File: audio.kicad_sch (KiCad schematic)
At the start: 23 parts, among them IC1 ES9218PQ, Y1 50MHz

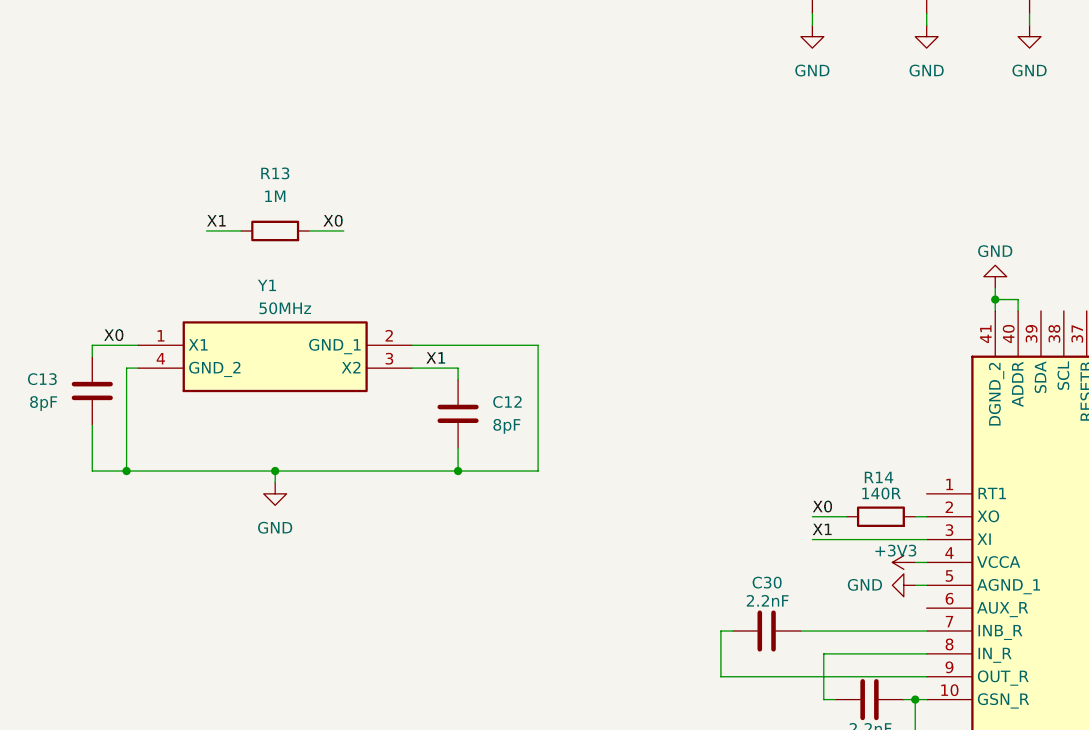
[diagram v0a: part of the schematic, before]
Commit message: changed the crystal for an oscillator, still dont know what to do wit XO pin
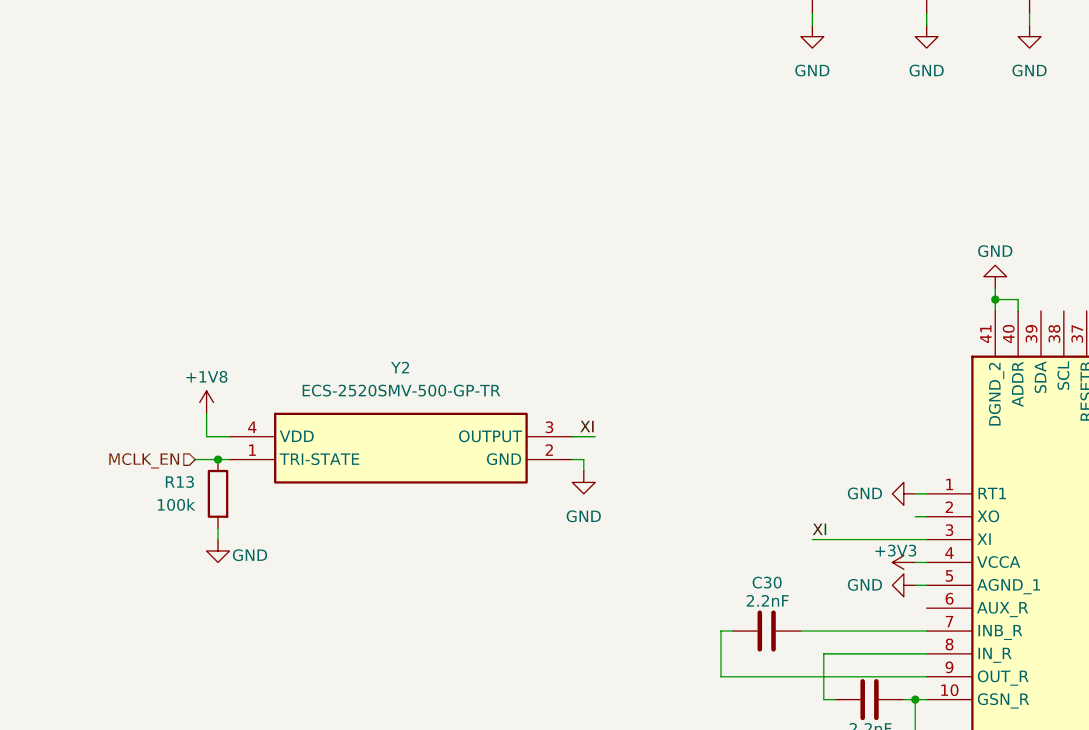
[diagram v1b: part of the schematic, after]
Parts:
- removed C12, C13: 8pF, symbol Device:C
- removed R14: 140R, symbol Device:R
- removed Y1: 50MHz, ABM10W240000MHZ8K1ZT3, symbol ABM10W-50.0000MHZ-4-B1U-T3:ABM10W-50.0000MHZ-4-B1U-T3
- added Y2: ECS-2520SMV-500-GP-TR, ECS2520SMV500GPTR, symbol ECS-2520SMV-500-GP-TR:ECS-2520SMV-500-GP-TR
- R13: value 1M -> 100k
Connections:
- net X0 is gone; now on net GND: R13.2
- net +1V8: now also Y2.4 (VDD)
- net GND: now also IC1.1 (RT1), Y2.2 (GND)
- net X1 renamed MCLK_EN
- net MCLK_EN: now also Y2.1 (TRI-STATE); no longer IC1.3 (XI)
- new net XI: IC1.3 (XI), Y2.3 (OUTPUT)

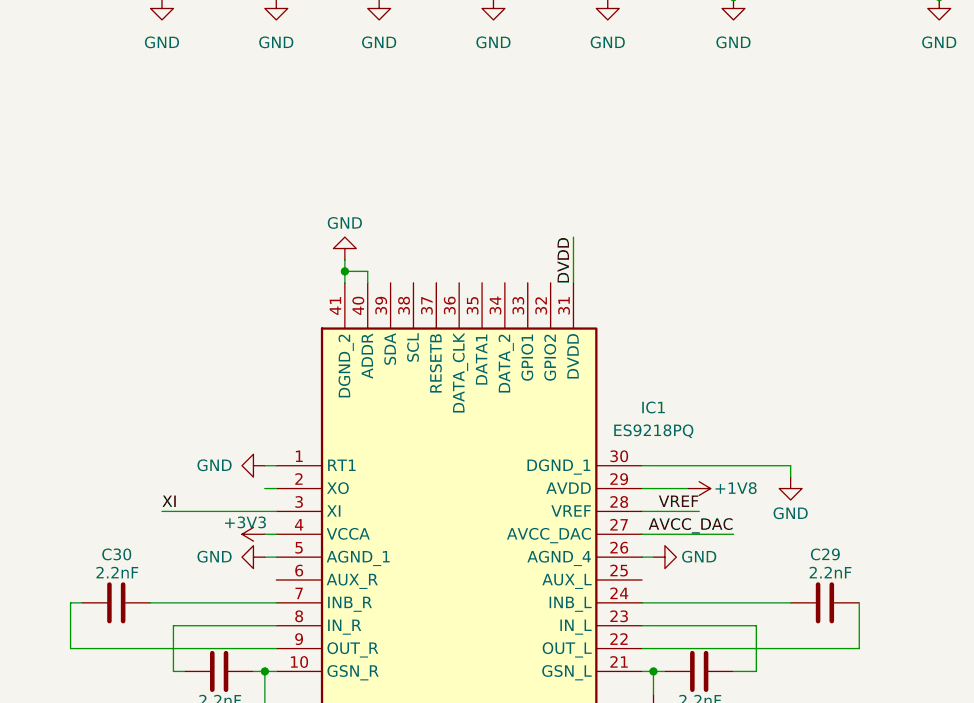
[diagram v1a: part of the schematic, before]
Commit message: added the sd card slot
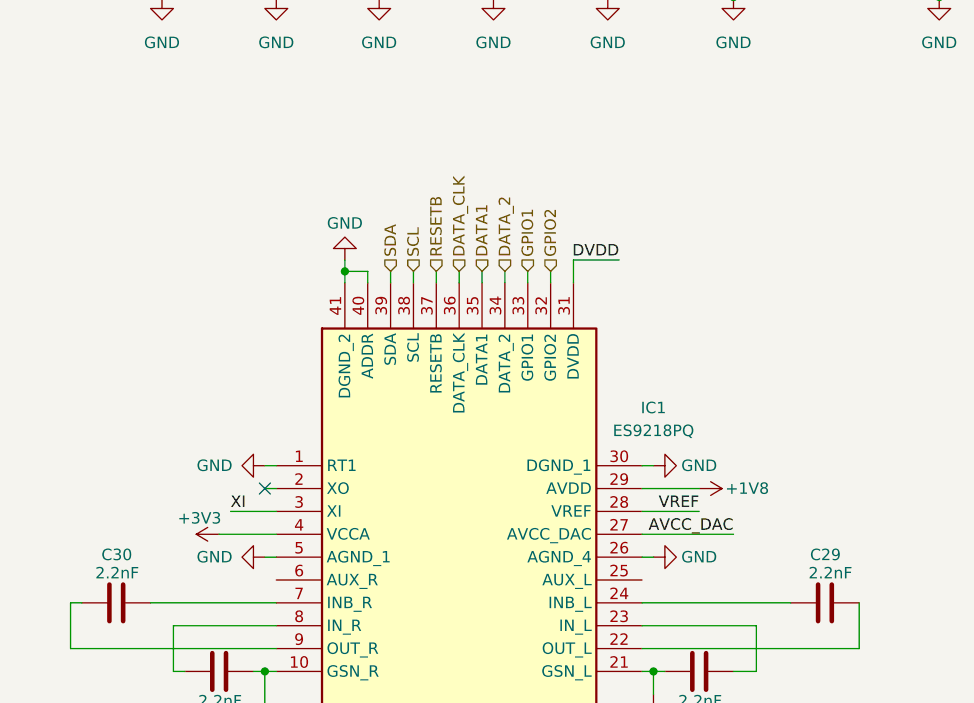
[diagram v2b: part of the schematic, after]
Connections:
- net GPIO2: now reaches IC1.32 (GPIO2)
- net GPIO1: now reaches IC1.33 (GPIO1)
- net DATA_2: now reaches IC1.34 (DATA_2)
- net DATA1: now reaches IC1.35 (DATA1)
- net DATA_CLK: now reaches IC1.36 (DATA_CLK)
- net RESETB: now reaches IC1.37 (RESETB)
- net SCL: now reaches IC1.38 (SCL)
- net SDA: now reaches IC1.39 (SDA)
- no-connect marks 0 -> 1

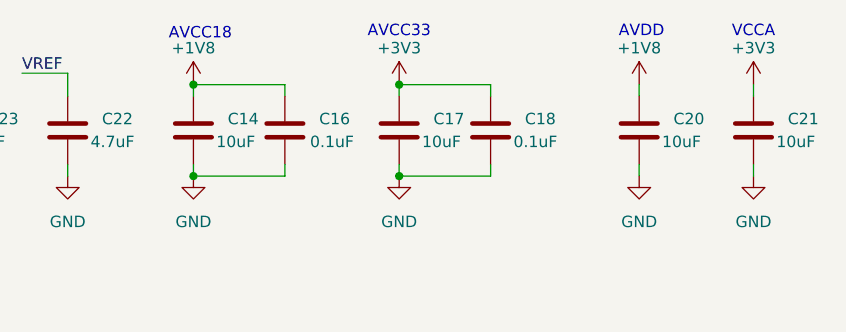
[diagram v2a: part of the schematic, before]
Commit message: made the jouranl complient, back-journaled
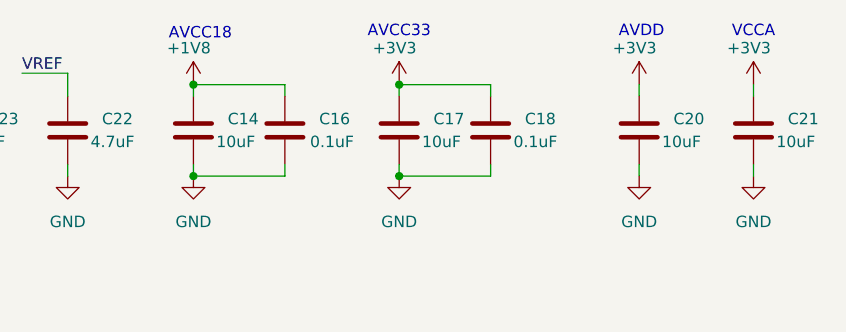
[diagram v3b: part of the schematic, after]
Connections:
- net +1V8: no longer C20.1
- net +3V3: now also C20.1
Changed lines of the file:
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@@
-	)
-	(symbol
-		(lib_id "power:+1V8")
-		(at 226.06 31.75 0)
-		(unit 1)
-		(exclude_from_sim no)
-		(in_bom yes)
-		(on_board yes)
-		(dnp no)
-		(property "Reference" "#PWR031"
-			(at 226.06 35.56 0)
-			(effects
-				(font
-					(size 1.27 1.27)
-				)
-				(hide yes)
-			)
-		)
-		(property "Value" "+1V8"
-			(at 226.06 27.686 0)
-			(effects
-				(font
-					(size 1.27 1.27)
-				)
-			)
-		)
-		(property "Footprint" ""
-			(at 226.06 31.75 0)
-			(effects
-				(font
-					(size 1.27 1.27)
-				)
-				(hide yes)
-			)
-		)
-		(property "Datasheet" ""
-			(at 226.06 31.75 0)
-			(effects
-				(font
-					(size 1.27 1.27)
-				)
-				(hide yes)
-			)
-		)
-		(property "Description" "Power symbol creates a global label with name \"+1V8\""
-			(at 226.06 31.75 0)
-			(effects
-				(font
-					(size 1.27 1.27)
-				)
-				(hide yes)
-			)
-		)
-		(pin "1"
-		)
-		(instances
-			(project "meko-pcb"
-				(path "/bdd43acd-23c1-472b-909a-8e24eb60d56d/dd2be10c-708f-4995-b13e-6fc09628a9ce"
-					(reference "#PWR031")
-					(unit 1)
-				)
-			)
-		)
 	)
 	(symbol
@@
 	)
 	(symbol
+		(lib_id "power:+3V3")
+		(at 226.06 31.75 0)
+		(unit 1)
+		(exclude_from_sim no)
+		(in_bom yes)
+		(on_board yes)
+		(dnp no)
+		(property "Reference" "#PWR03"
+			(at 226.06 35.56 0)
+			(effects
+				(font
+					(size 1.27 1.27)
+				)
+				(hide yes)
+			)
+		)
+		(property "Value" "+3V3"
+			(at 225.552 27.686 0)
+			(effects
+				(font
+					(size 1.27 1.27)
+				)
+			)
+		)
+		(property "Footprint" ""
+			(at 226.06 31.75 0)
+			(effects
+				(font
+					(size 1.27 1.27)
+				)
+				(hide yes)
+			)
+		)
+		(property "Datasheet" ""
+			(at 226.06 31.75 0)
+			(effects
+				(font
+					(size 1.27 1.27)
+				)
+				(hide yes)
+			)
+		)
+		(property "Description" "Power symbol creates a global label with name \"+3V3\""
+			(at 226.06 31.75 0)
+			(effects
+				(font
+					(size 1.27 1.27)
+				)
+				(hide yes)
+			)
+		)
+		(pin "1"
+		)
+		(instances
+			(project "meko-pcb"
+				(path "/bdd43acd-23c1-472b-909a-8e24eb60d56d/dd2be10c-708f-4995-b13e-6fc09628a9ce"
+					(reference "#PWR03")
+					(unit 1)
+				)
+			)
+		)
+	)
+	(symbol
 		(lib_id "Device:C")
 		(at 149.86 36.83 0)
@@
 			)
 		)
-		(property "Datasheet" "https://ecsxtal.com/store/pdf/ECS-2520SMV.pdf"
+		(property "Datasheet" "https://eu.mouser.com/datasheet/2/122/ECS_2520SMV-1628252.pdf"
 			(at 82.55 282.55 0)
 			(effects
@@
 		)
 		(property "Value" "+1V8"
-			(at 176.53 27.686 0)
+			(at 176.022 27.686 0)
 			(effects
 				(font
@@
 		)
 		(property "Value" "+3V3"
-			(at 199.39 27.686 0)
+			(at 198.882 27.686 0)
 			(effects
 				(font
@@
 		)
 		(property "Value" "+3V3"
-			(at 238.76 27.686 0)
-			(effects
-				(font
+			(at 238.252 27.686 0)
+			(effects
+				(font

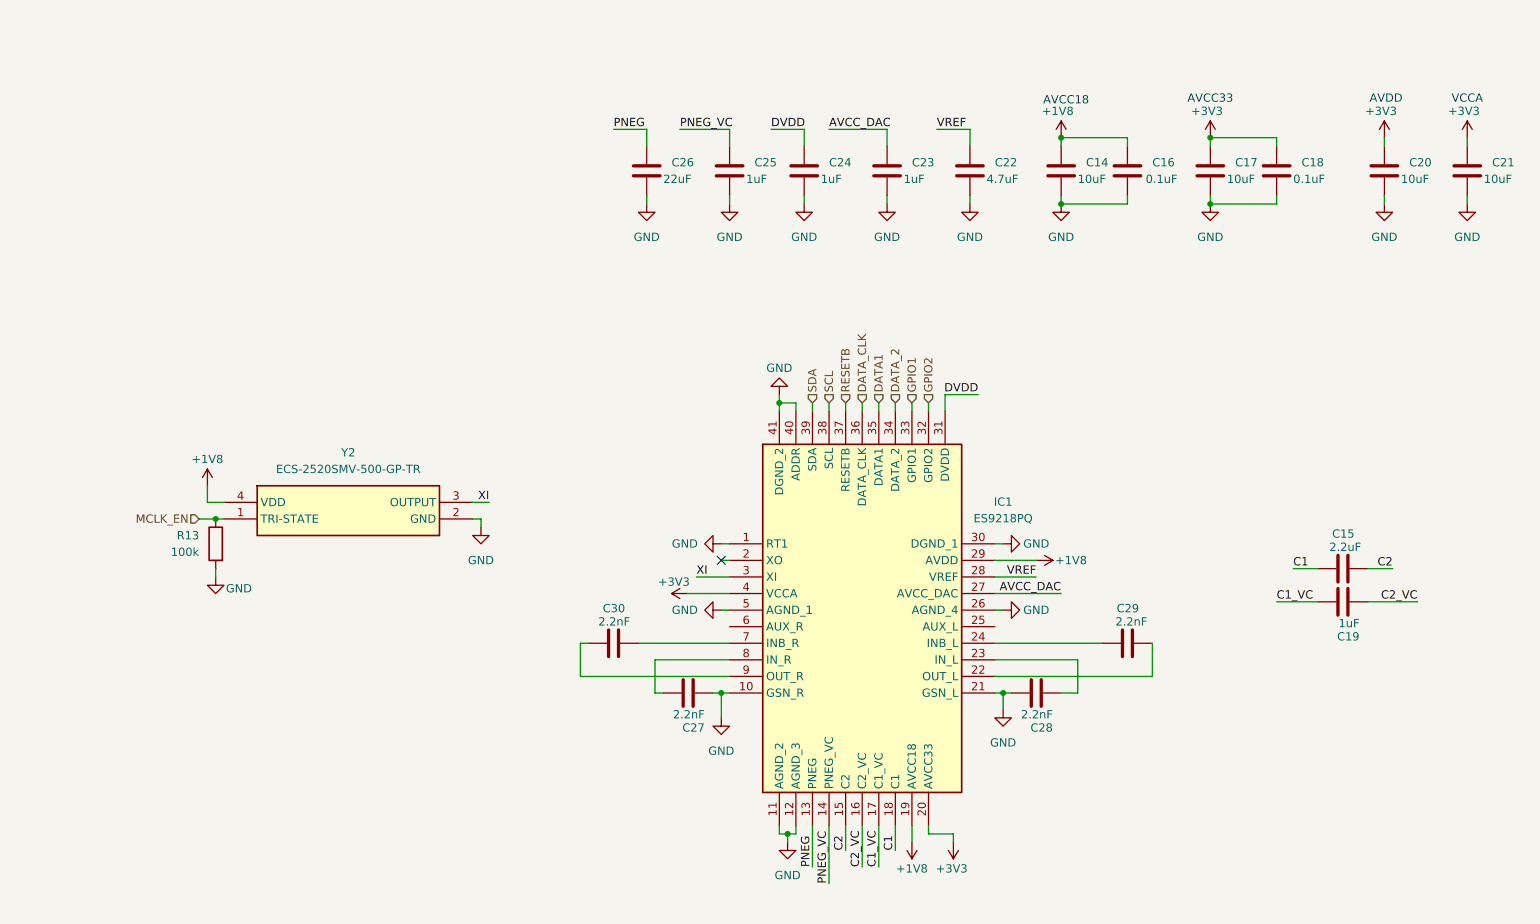
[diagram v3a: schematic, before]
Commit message: re-did power with the new small LDOs and power system
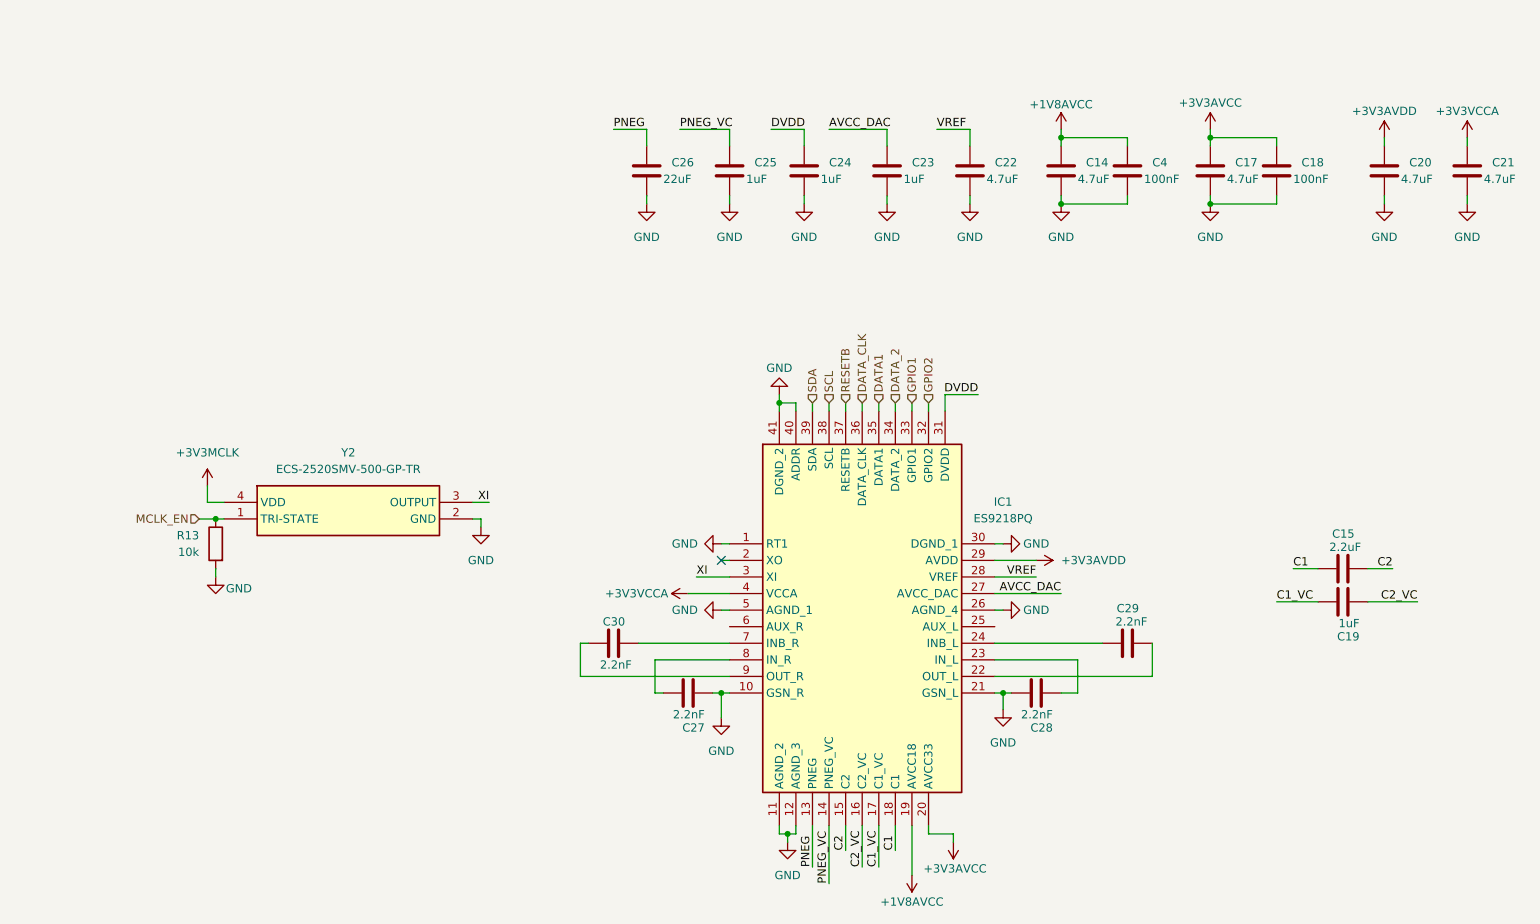
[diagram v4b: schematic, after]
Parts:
- removed C16: 0.1uF, symbol Device:C
- added C4: 100nF, symbol Device:C
- C14, C17, C20, C21: value 10uF -> 4.7uF
- C18: value 0.1uF -> 100nF
- R13: value 100k -> 10k
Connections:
- net GND: now also C4.2
- net +1V8 renamed +1V8AVCC
- net +1V8AVCC: now also C4.1; no longer IC1.29 (AVDD), Y2.4 (VDD)
- net +3V3 renamed +3V3AVCC
- net +3V3AVCC: no longer C20.1, C21.1, IC1.4 (VCCA)
- new net +3V3AVDD: C20.1, IC1.29 (AVDD)
- new net +3V3MCLK: Y2.4 (VDD)
- new net +3V3VCCA: C21.1, IC1.4 (VCCA)
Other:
- note removed: "AVCC18"
- note removed: "AVCC33"
- note removed: "AVDD"
- note removed: "VCCA"

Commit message: created custom symbol for the display, added pull-up/-down resistors
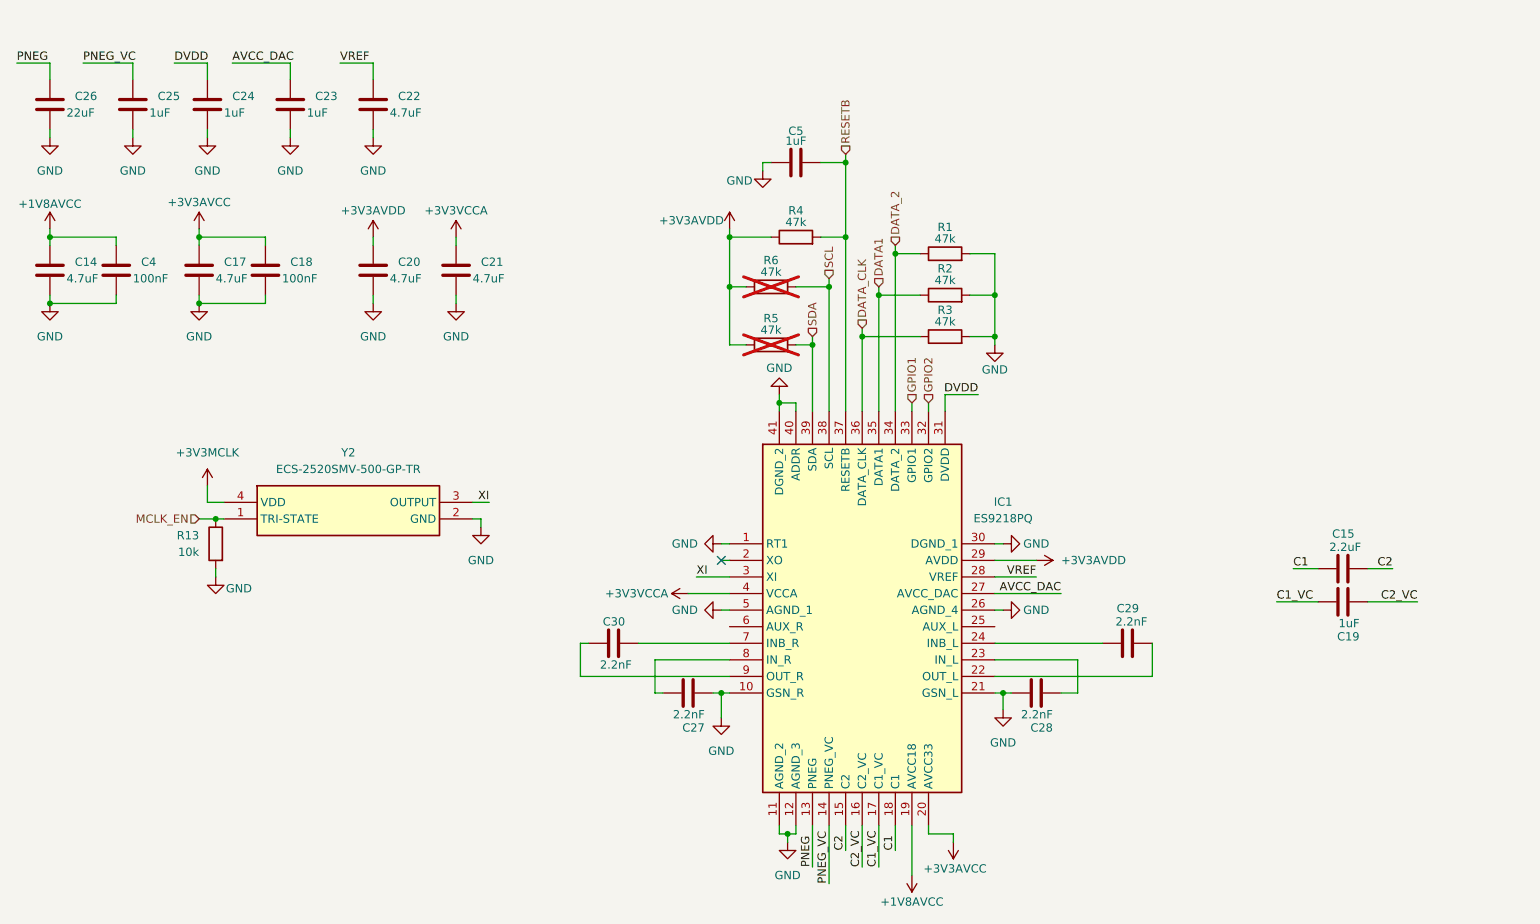
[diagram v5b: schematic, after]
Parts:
- added C5: 1uF, symbol Device:C
- added R1, R2, R3, R4, R5, R6: 47k, symbol Device:R
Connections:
- net +3V3AVDD: now also R4.1, R5.1, R6.1
- net DATA1: now also R2.1
- net DATA_2: now also R1.1
- net DATA_CLK: now also R3.1
- net GND: now also C5.1, R1.2, R2.2, R3.2
- net RESETB: now also C5.2, R4.2
- net SCL: now also R6.2
- net SDA: now also R5.2
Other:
- moved on the sheet: C14, C17, C18, C20, C21, C22, C23, C24, C25, C26, C4

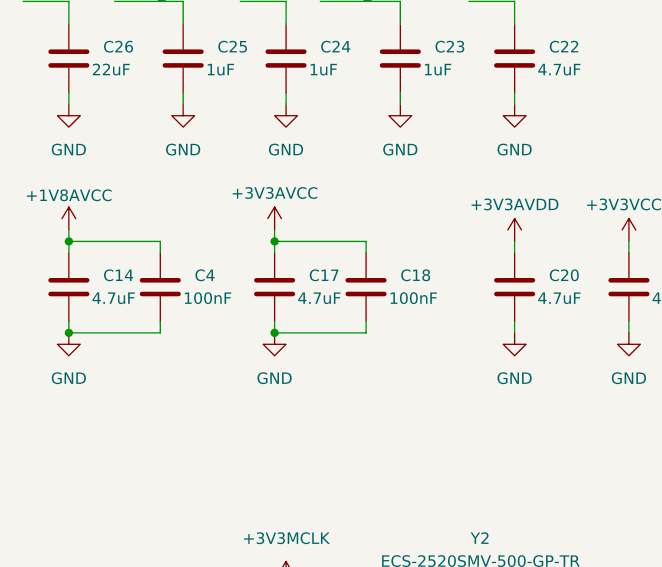
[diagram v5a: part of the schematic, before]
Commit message: i2c, i2s, uart, en, sd card
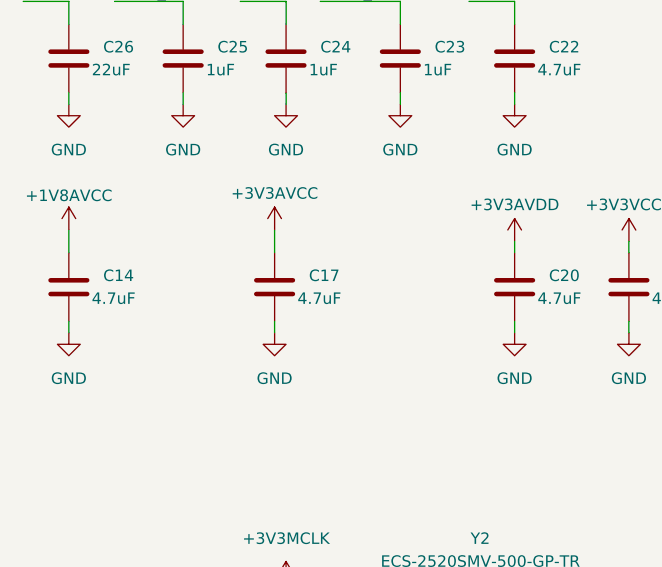
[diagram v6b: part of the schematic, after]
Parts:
- removed C18, C4: 100nF, symbol Device:C
